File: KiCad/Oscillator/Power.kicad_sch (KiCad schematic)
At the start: 10 parts, among them U1 40106, U2 TL074

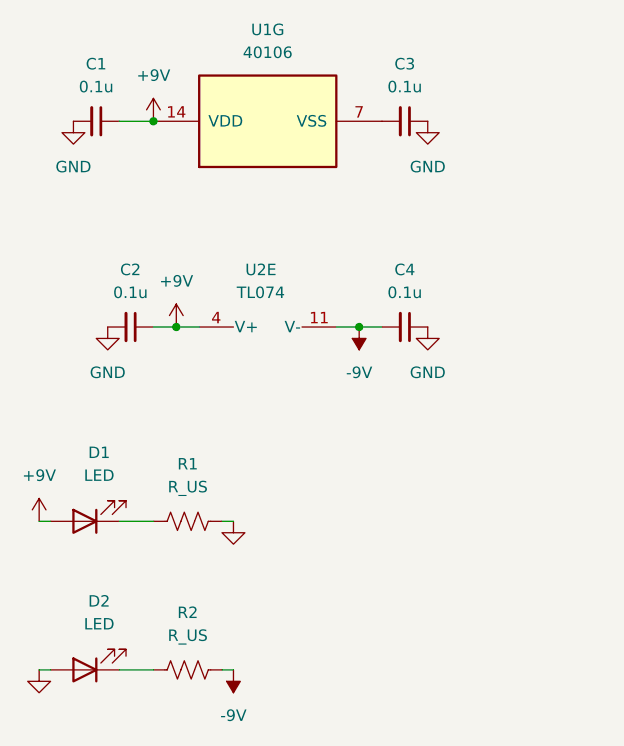
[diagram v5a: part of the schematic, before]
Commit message: updated footprints in oscillator
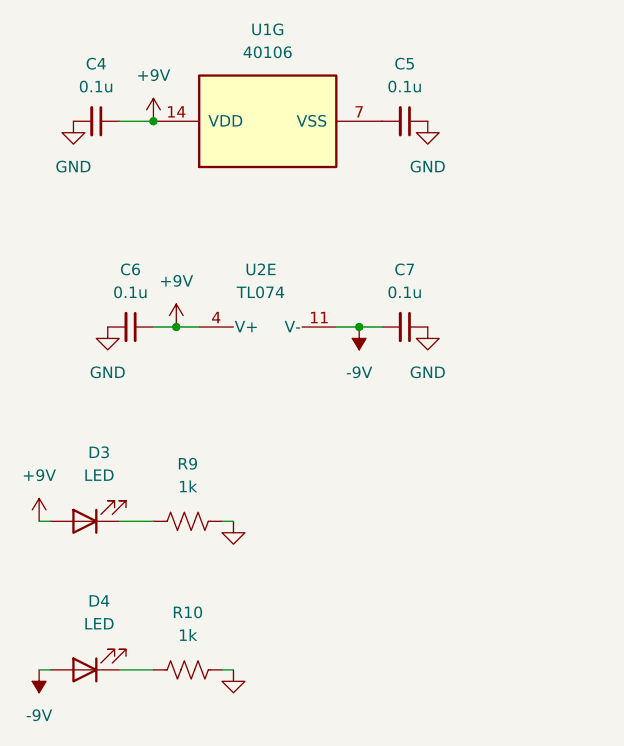
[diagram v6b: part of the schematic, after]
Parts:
- C4: renamed from C1; footprint Capacitor_SMD:C_0603_1608Metric -> Capacitor_SMD:C_0805_2012Metric
- C5: renamed from C3; footprint Capacitor_SMD:C_0603_1608Metric -> Capacitor_SMD:C_0805_2012Metric
- C6: renamed from C2; footprint Capacitor_SMD:C_0603_1608Metric -> Capacitor_SMD:C_0805_2012Metric
- C7: renamed from C4; footprint Capacitor_SMD:C_0603_1608Metric -> Capacitor_SMD:C_0805_2012Metric
- D3: renamed from D1; footprint (none) -> LED_THT:LED_D5.0mm
- D4: renamed from D2; footprint (none) -> LED_THT:LED_D5.0mm
- R10: renamed from R2; value R_US -> 1k; footprint (none) -> Resistor_SMD:R_0805_2012Metric
- R9: renamed from R1; value R_US -> 1k; footprint (none) -> Resistor_SMD:R_0805_2012Metric
- U1: footprint Schmitt Inv. CD40106BE:N14 -> Package_DIP:DIP-14_W7.62mm
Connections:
- net -9V: now also D4.2 (A); no longer R10.2
- net GND: now also R10.2; no longer D4.2 (A)
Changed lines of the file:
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@@
 		(dnp no)
 		(fields_autoplaced yes)
-		(property "Reference" "#PWR011"
+		(property "Reference" "#PWR033"
 			(at 63.5 73.66 0)
 			(hide yes)
@@
 			)
 		)
-		(property "Footprint" "Schmitt Inv. CD40106BE:N14"
+		(property "Footprint" "Package_DIP:DIP-14_W7.62mm"
 			(at 45.72 44.45 0)
 			(hide yes)
@@
 		(dnp no)
 		(fields_autoplaced yes)
-		(property "Reference" "#PWR06"
+		(property "Reference" "#PWR031"
 			(at 35.56 71.12 0)
 			(hide yes)
@@
 		(dnp no)
 		(fields_autoplaced yes)
-		(property "Reference" "R1"
+		(property "Reference" "R9"
 			(at 36.83 82.55 90)
 			(show_name no)
@@
 			)
 		)
-		(property "Value" "R_US"
+		(property "Value" "1k"
 			(at 36.83 85.09 90)
 			(show_name no)
@@
 			)
 		)
-		(property "Footprint" ""
+		(property "Footprint" "Resistor_SMD:R_0805_2012Metric"
 			(at 37.084 87.884 90)
 			(hide yes)
@@
 				(path "/30119ed2-ce55-41fd-b608-3963355ff01b"
 					(reference "R1")
+					(unit 1)
+				)
+			)
+			(project "Oscillator"
+				(path "/3ca3a63e-46c1-4b14-be30-fce478aad491"
+					(reference "R9")
 					(unit 1)
 				)
@@
 		(dnp no)
 		(fields_autoplaced yes)
-		(property "Reference" "C3"
+		(property "Reference" "C5"
 			(at 60.9536 38.1 90)
 			(show_name no)
@@
 			)
 		)
-		(property "Footprint" "Capacitor_SMD:C_0603_1608Metric"
+		(property "Footprint" "Capacitor_SMD:C_0805_2012Metric"
 			(at 60.96 44.45 0)
 			(hide yes)
@@
 		(dnp no)
 		(fields_autoplaced yes)
-		(property "Reference" "#PWR013"
+		(property "Reference" "#PWR027"
 			(at 114.3 63.5 0)
 			(hide yes)
@@
 		(dnp no)
 		(fields_autoplaced yes)
-		(property "Reference" "#PWR07"
+		(property "Reference" "#PWR035"
 			(at 41.91 95.25 0)
 			(hide yes)
@@
 				)
 			)
+			(project "Oscillator"
+				(path "/3ca3a63e-46c1-4b14-be30-fce478aad491"
+					(reference "#PWR035")
+					(unit 1)
+				)
+			)
 		)
 	)
 	(symbol
 		(lib_id "power:GND")
-		(at 20.32 105.41 0)
+		(at 41.91 105.41 0)
 		(unit 1)
 		(body_style 1)
@@
 		(dnp no)
 		(fields_autoplaced yes)
-		(property "Reference" "#PWR02"
-			(at 20.32 111.76 0)
+		(property "Reference" "#PWR037"
+			(at 41.91 111.76 0)
 			(hide yes)
 			(show_name no)
@@
 		)
 		(property "Value" "GND"
-			(at 20.32 110.49 0)
+			(at 41.91 110.49 0)
 			(hide yes)
 			(show_name no)
@@
 		)
 		(property "Footprint" ""
-			(at 20.32 105.41 0)
+			(at 41.91 105.41 0)
 			(hide yes)
 			(show_name no)
@@
 		)
 		(property "Datasheet" ""
-			(at 20.32 105.41 0)
+			(at 41.91 105.41 0)
 			(hide yes)
 			(show_name no)
@@
 		)
 		(property "Description" "Power symbol creates a global label with name \"GND\" , ground"
-			(at 20.32 105.41 0)
+			(at 41.91 105.41 0)
 			(hide yes)
 			(show_name no)
@@
 				(path "/30119ed2-ce55-41fd-b608-3963355ff01b"
 					(reference "#PWR02")
+					(unit 1)
+				)
+			)
+			(project "Oscillator"
+				(path "/3ca3a63e-46c1-4b14-be30-fce478aad491"
+					(reference "#PWR037")
 					(unit 1)
 				)
@@
 		(dnp no)
 		(fields_autoplaced yes)
-		(property "Reference" "#PWR010"
+		(property "Reference" "#PWR025"
 			(at 63.5 50.8 0)
 			(hide yes)
@@
 		(dnp no)
 		(fields_autoplaced yes)
-		(property "Reference" "C1"
+		(property "Reference" "C4"
 			(at 26.6636 38.1 90)
 			(show_name no)
@@
 			)
 		)
-		(property "Footprint" "Capacitor_SMD:C_0603_1608Metric"
+		(property "Footprint" "Capacitor_SMD:C_0805_2012Metric"
 			(at 26.67 44.45 0)
 			(hide yes)
@@
 		(dnp no)
 		(fields_autoplaced yes)
-		(property "Reference" "D1"
+		(property "Reference" "D3"
 			(at 26.9875 81.28 0)
 			(show_name no)
@@
 			)
 		)
-		(property "Footprint" ""
+		(property "Footprint" "LED_THT:LED_D5.0mm"
 			(at 25.4 88.9 0)
 			(hide yes)
@@
 				(path "/30119ed2-ce55-41fd-b608-3963355ff01b"
 					(reference "D1")
+					(unit 1)
+				)
+			)
+			(project "Oscillator"
+				(path "/3ca3a63e-46c1-4b14-be30-fce478aad491"
+					(reference "D3")
 					(unit 1)
 				)
@@
 		(dnp no)
 		(fields_autoplaced yes)
-		(property "Reference" "#PWR01"
+		(property "Reference" "#PWR034"
 			(at 20.32 92.71 0)
 			(hide yes)
@@
 				(path "/30119ed2-ce55-41fd-b608-3963355ff01b"
 					(reference "#PWR01")
+					(unit 1)
+				)
+			)
+			(project "Oscillator"
+				(path "/3ca3a63e-46c1-4b14-be30-fce478aad491"
+					(reference "#PWR034")
 					(unit 1)
 				)
@@
 		(dnp no)
 		(fields_autoplaced yes)
-		(property "Reference" "#PWR012"
+		(property "Reference" "#PWR026"
 			(at 95.25 63.5 0)
 			(hide yes)
@@
 			)
 		)
-		(property "Footprint" "Schmitt Inv. CD40106BE:N14"
+		(property "Footprint" "Package_DIP:DIP-14_W7.62mm"
 			(at 140.97 57.15 0)
 			(hide yes)
@@
 		(dnp no)
 		(fields_autoplaced yes)
-		(property "Reference" "#PWR04"
+		(property "Reference" "#PWR030"
 			(at 27.94 73.66 0)
 			(hide yes)
@@
 		(dnp no)
 		(fields_autoplaced yes)
-		(property "Reference" "#PWR014"
+		(property "Reference" "#PWR028"
 			(at 133.35 63.5 0)
 			(hide yes)
@@
 			)
 		)
-		(property "Footprint" "Schmitt Inv. CD40106BE:N14"
+		(property "Footprint" "Package_DIP:DIP-14_W7.62mm"
 			(at 160.02 57.15 0)
 			(hide yes)
@@
 		(dnp no)
 		(fields_autoplaced yes)
-		(property "Reference" "#PWR05"
+		(property "Reference" "#PWR024"
 			(at 33.02 48.26 0)
 			(hide yes)
@@
 		(dnp no)
 		(fields_autoplaced yes)
-		(property "Reference" "C4"
+		(property "Reference" "C7"
 			(at 60.9536 60.96 90)
 			(show_name no)
@@
 			)
 		)
-		(property "Footprint" "Capacitor_SMD:C_0603_1608Metric"
+		(property "Footprint" "Capacitor_SMD:C_0805_2012Metric"
 			(at 60.96 67.31 0)
 			(hide yes)
@@
 			)
 		)
-		(property "Footprint" "Schmitt Inv. CD40106BE:N14"
+		(property "Footprint" "Package_DIP:DIP-14_W7.62mm"
 			(at 121.92 57.15 0)
 			(hide yes)
@@
 		(dnp no)
 		(fields_autoplaced yes)
-		(property "Reference" "R2"
+		(property "Reference" "R10"
 			(at 36.83 99.06 90)
 			(show_name no)
@@
 			)
 		)
-		(property "Value" "R_US"
+		(property "Value" "1k"
 			(at 36.83 101.6 90)
 			(show_name no)
@@
 			)
 		)
-		(property "Footprint" ""
+		(property "Footprint" "Resistor_SMD:R_0805_2012Metric"
 			(at 37.084 104.394 90)
 			(hide yes)
@@
 				(path "/30119ed2-ce55-41fd-b608-3963355ff01b"
 					(reference "R2")
+					(unit 1)
+				)
+			)
+			(project "Oscillator"
+				(path "/3ca3a63e-46c1-4b14-be30-fce478aad491"
+					(reference "R10")
 					(unit 1)
 				)
@@
 		(dnp no)
 		(fields_autoplaced yes)
-		(property "Reference" "#PWR015"
+		(property "Reference" "#PWR029"
 			(at 152.4 63.5 0)
 			(hide yes)
@@
 		(dnp no)
 		(fields_autoplaced yes)
-		(property "Reference" "D2"
+		(property "Reference" "D4"
 			(at 26.9875 97.79 0)
 			(show_name no)
@@
 			)
 		)
-		(property "Footprint" ""
+		(property "Footprint" "LED_THT:LED_D5.0mm"
 			(at 25.4 105.41 0)
 			(hide yes)
@@
 				(path "/30119ed2-ce55-41fd-b608-3963355ff01b"
 					(reference "D2")
+					(unit 1)
+				)
+			)
+			(project "Oscillator"
+				(path "/3ca3a63e-46c1-4b14-be30-fce478aad491"
+					(reference "D4")
 					(unit 1)
 				)
@@
 		(dnp no)
 		(fields_autoplaced yes)
-		(property "Reference" "C2"
+		(property "Reference" "C6"
 			(at 30.4736 60.96 90)
 			(show_name no)
@@
 			)
 		)
-		(property "Footprint" "Capacitor_SMD:C_0603_1608Metric"
+		(property "Footprint" "Capacitor_SMD:C_0805_2012Metric"
 			(at 30.48 67.31 0)
 			(hide yes)
@@
 		(dnp no)
 		(fields_autoplaced yes)
-		(property "Reference" "#PWR09"
+		(property "Reference" "#PWR032"
 			(at 55.88 63.5 0)
 			(hide yes)
@@
 			)
 		)
-		(property "Footprint" "Schmitt Inv. CD40106BE:N14"
+		(property "Footprint" "Package_DIP:DIP-14_W7.62mm"
 			(at 102.87 57.15 0)
 			(hide yes)
@@
 	(symbol
 		(lib_id "power:-9V")
-		(at 41.91 105.41 180)
+		(at 20.32 105.41 180)
 		(unit 1)
 		(body_style 1)
@@
 		(dnp no)
 		(fields_autoplaced yes)
-		(property "Reference" "#PWR08"
-			(at 41.91 101.6 0)
+		(property "Reference" "#PWR036"
+			(at 20.32 101.6 0)
 			(hide yes)
 			(show_name no)
@@
 		)
 		(property "Value" "-9V"
-			(at 41.91 110.49 0)
+			(at 20.32 110.49 0)
 			(show_name no)
 			(do_not_autoplace no)
@@
 		)
 		(property "Footprint" ""
-			(at 41.91 105.41 0)
+			(at 20.32 105.41 0)
 			(hide yes)
 			(show_name no)
@@
 		)
 		(property "Datasheet" ""
-			(at 41.91 105.41 0)
+			(at 20.32 105.41 0)
 			(hide yes)
 			(show_name no)
@@
 		)
 		(property "Description" "Power symbol creates a global label with name \"-9V\""
-			(at 41.91 105.41 0)
+			(at 20.32 105.41 0)
 			(hide yes)
 			(show_name no)
@@
 				(path "/30119ed2-ce55-41fd-b608-3963355ff01b"
 					(reference "#PWR08")
+					(unit 1)
+				)
+			)
+			(project "Oscillator"
+				(path "/3ca3a63e-46c1-4b14-be30-fce478aad491"
+					(reference "#PWR036")
 					(unit 1)
 				)
@@
 		(dnp no)
 		(fields_autoplaced yes)
-		(property "Reference" "#PWR03"
+		(property "Reference" "#PWR023"
 			(at 24.13 50.8 0)
 			(hide yes)
@@
 		)
 	)
-	(embedded_fonts no)
 )

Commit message: oscillator pcb layout done
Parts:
- removed C5: 0.1u, Capacitor_SMD:C_0805_2012Metric, symbol Device:C_Small
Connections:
- net GND: now also U1.1, U1.3, U1.7 (VSS); no longer U1.3, U1.5
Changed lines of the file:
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@@
 		(property "Value" "GND"
 			(at 63.5 72.39 0)
+			(hide yes)
 			(show_name no)
 			(do_not_autoplace no)
@@
 	)
 	(symbol
-		(lib_id "Device:C_Small")
-		(at 60.96 44.45 270)
-		(unit 1)
-		(body_style 1)
-		(exclude_from_sim no)
-		(in_bom yes)
-		(on_board yes)
-		(in_pos_files yes)
-		(dnp no)
-		(fields_autoplaced yes)
-		(property "Reference" "C5"
-			(at 60.9536 38.1 90)
-			(show_name no)
-			(do_not_autoplace no)
-			(effects
-				(font
-					(size 1.27 1.27)
-				)
-			)
-		)
-		(property "Value" "0.1u"
-			(at 60.9536 40.64 90)
-			(show_name no)
-			(do_not_autoplace no)
-			(effects
-				(font
-					(size 1.27 1.27)
-				)
-			)
-		)
-		(property "Footprint" "Capacitor_SMD:C_0805_2012Metric"
-			(at 60.96 44.45 0)
-			(hide yes)
-			(show_name no)
-			(do_not_autoplace no)
-			(effects
-				(font
-					(size 1.27 1.27)
-				)
-			)
-		)
-		(property "Datasheet" ""
-			(at 60.96 44.45 0)
-			(hide yes)
-			(show_name no)
-			(do_not_autoplace no)
-			(effects
-				(font
-					(size 1.27 1.27)
-				)
-			)
-		)
-		(property "Description" "Unpolarized capacitor, small symbol"
-			(at 60.96 44.45 0)
-			(hide yes)
-			(show_name no)
-			(do_not_autoplace no)
-			(effects
-				(font
-					(size 1.27 1.27)
-				)
-			)
-		)
-		(property "LCSC Part #" ""
-			(at 60.96 44.45 90)
-			(hide yes)
-			(show_name no)
-			(do_not_autoplace no)
-			(effects
-				(font
-					(size 1.27 1.27)
-				)
-			)
-		)
-		(pin "1"
-		)
-		(pin "2"
-		)
-		(instances
-			(project "Power"
-				(path "/30119ed2-ce55-41fd-b608-3963355ff01b"
-					(reference "C3")
-					(unit 1)
-				)
-			)
-			(project "Oscillator"
-				(path "/3ca3a63e-46c1-4b14-be30-fce478aad491"
-					(reference "C5")
-					(unit 1)
-				)
-			)
-		)
-	)
-	(symbol
 		(lib_id "power:GND")
 		(at 114.3 57.15 0)
@@
 		(property "Value" "GND"
 			(at 114.3 62.23 0)
+			(hide yes)
 			(show_name no)
 			(do_not_autoplace no)
@@
 	(symbol
 		(lib_id "power:GND")
-		(at 63.5 44.45 0)
+		(at 58.42 44.45 0)
 		(unit 1)
 		(body_style 1)
@@
 		(fields_autoplaced yes)
 		(property "Reference" "#PWR025"
-			(at 63.5 50.8 0)
+			(at 58.42 50.8 0)
 			(hide yes)
 			(show_name no)
@@
 		)
 		(property "Value" "GND"
-			(at 63.5 49.53 0)
+			(at 58.42 49.53 0)
+			(hide yes)
 			(show_name no)
 			(do_not_autoplace no)
@@
 		)
 		(property "Footprint" ""
-			(at 63.5 44.45 0)
+			(at 58.42 44.45 0)
 			(hide yes)
 			(show_name no)
@@
 		)
 		(property "Datasheet" ""
-			(at 63.5 44.45 0)
+			(at 58.42 44.45 0)
 			(hide yes)
 			(show_name no)
@@
 		)
 		(property "Description" "Power symbol creates a global label with name \"GND\" , ground"
-			(at 63.5 44.45 0)
+			(at 58.42 44.45 0)
 			(hide yes)
 			(show_name no)
@@
 		(property "Value" "GND"
 			(at 95.25 62.23 0)
+			(hide yes)
 			(show_name no)
 			(do_not_autoplace no)
@@
 		(property "Value" "GND"
 			(at 27.94 72.39 0)
+			(hide yes)
 			(show_name no)
 			(do_not_autoplace no)
@@
 		(property "Value" "GND"
 			(at 133.35 62.23 0)
+			(hide yes)
 			(show_name no)
 			(do_not_autoplace no)
@@
 		(lib_id "4xxx:40106")
 		(at 121.92 57.15 0)
-		(unit 3)
+		(unit 2)
 		(body_style 1)
 		(exclude_from_sim no)
@@
 				(path "/3ca3a63e-46c1-4b14-be30-fce478aad491"
 					(reference "U1")
-					(unit 3)
+					(unit 2)
 				)
 			)
@@
 		(property "Value" "GND"
 			(at 152.4 62.23 0)
+			(hide yes)
 			(show_name no)
 			(do_not_autoplace no)
@@
 		(lib_id "4xxx:40106")
 		(at 102.87 57.15 0)
-		(unit 2)
+		(unit 1)
 		(body_style 1)
 		(exclude_from_sim no)
@@
 				(path "/3ca3a63e-46c1-4b14-be30-fce478aad491"
 					(reference "U1")
-					(unit 2)
+					(unit 1)
 				)
 			)
@@
 		(property "Value" "GND"
 			(at 24.13 49.53 0)
-			(show_name no)
-			(do_not_autoplace no)
+			(hide yes)
+			(show_name no)
+			(do_not_autoplace no)

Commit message: preparation to merge project back into one board
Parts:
- C4, C6, C7, R10, R9: KiLib_Generator (none) -> SMD_2terminal_chip_molded
- D3, D4: KiLib_Generator (none) -> LED/THT
- U1, U2: KiLib_Generator (none) -> package/DIP/legacy
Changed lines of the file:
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@@
+			)
+		)
+		(property "KiLib_Generator" "package/DIP/legacy"
+			(at 45.72 44.45 0)
+			(hide yes)
+			(show_name no)
+			(do_not_autoplace no)
+			(effects
+				(font
+					(size 1.27 1.27)
+				)
 			)
 		)
@@
 			)
 		)
+		(property "KiLib_Generator" "SMD_2terminal_chip_molded"
+			(at 36.83 88.9 0)
+			(hide yes)
+			(show_name no)
+			(do_not_autoplace no)
+			(effects
+				(font
+					(size 1.27 1.27)
+				)
+			)
+		)
 		(pin "1"
 		)
@@
 			)
 		)
+		(property "KiLib_Generator" "SMD_2terminal_chip_molded"
+			(at 26.67 44.45 0)
+			(hide yes)
+			(show_name no)
+			(do_not_autoplace no)
+			(effects
+				(font
+					(size 1.27 1.27)
+				)
+			)
+		)
 		(pin "1"
 		)
@@
 			)
 		)
+		(property "KiLib_Generator" "LED/THT"
+			(at 25.4 88.9 0)
+			(hide yes)
+			(show_name no)
+			(do_not_autoplace no)
+			(effects
+				(font
+					(size 1.27 1.27)
+				)
+			)
+		)
 		(pin "2"
 		)
@@
 		(property "LCSC Part #" ""
 			(at 45.72 64.77 90)
+			(hide yes)
+			(show_name no)
+			(do_not_autoplace no)
+			(effects
+				(font
+					(size 1.27 1.27)
+				)
+			)
+		)
+		(property "KiLib_Generator" "package/DIP/legacy"
+			(at 45.72 64.77 0)
 			(hide yes)
 			(show_name no)
@@
 			)
 		)
+		(property "KiLib_Generator" "package/DIP/legacy"
+			(at 140.97 57.15 0)
+			(hide yes)
+			(show_name no)
+			(do_not_autoplace no)
+			(effects
+				(font
+					(size 1.27 1.27)
+				)
+			)
+		)
 		(pin "1"
 		)
@@
 			)
 		)
+		(property "KiLib_Generator" "package/DIP/legacy"
+			(at 160.02 57.15 0)
+			(hide yes)
+			(show_name no)
+			(do_not_autoplace no)
+			(effects
+				(font
+					(size 1.27 1.27)
+				)
+			)
+		)
 		(pin "1"
 		)
@@
 			)
 		)
+		(property "KiLib_Generator" "SMD_2terminal_chip_molded"
+			(at 60.96 67.31 0)
+			(hide yes)
+			(show_name no)
+			(do_not_autoplace no)
+			(effects
+				(font
+					(size 1.27 1.27)
+				)
+			)
+		)
 		(pin "1"
 		)
@@
 			)
 		)
+		(property "KiLib_Generator" "package/DIP/legacy"
+			(at 121.92 57.15 0)
+			(hide yes)
+			(show_name no)
+			(do_not_autoplace no)
+			(effects
+				(font
+					(size 1.27 1.27)
+				)
+			)
+		)
 		(pin "1"
 		)
@@
 			)
 		)
+		(property "KiLib_Generator" "SMD_2terminal_chip_molded"
+			(at 36.83 105.41 0)
+			(hide yes)
+			(show_name no)
+			(do_not_autoplace no)
+			(effects
+				(font
+					(size 1.27 1.27)
+				)
+			)
+		)
 		(pin "1"
 		)
@@
 			)
 		)
+		(property "KiLib_Generator" "LED/THT"
+			(at 25.4 105.41 0)
+			(hide yes)
+			(show_name no)
+			(do_not_autoplace no)
+			(effects
+				(font
+					(size 1.27 1.27)
+				)
+			)
+		)
 		(pin "2"
 		)
@@
 			)
 		)
+		(property "KiLib_Generator" "SMD_2terminal_chip_molded"
+			(at 30.48 67.31 0)
+			(hide yes)
+			(show_name no)
+			(do_not_autoplace no)
+			(effects
+				(font
+					(size 1.27 1.27)
+				)
+			)
+		)
 		(pin "1"
 		)
@@
 			(at 102.87 57.15 0)
 			(hide yes)
+			(show_name no)
+			(do_not_autoplace no)
+			(effects
+				(font
+					(size 1.27 1.27)
+				)
+			)
+		)
+		(property "KiLib_Generator" "package/DIP/legacy"
+			(at 102.87 57.15 0)
+			(hide yes)
